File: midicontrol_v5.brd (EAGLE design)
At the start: 118.2 x 42.4 mm, 65 parts, among them SW1 EC12E_SW, U1 6N138S(TB), U3 74HC595D, U4 ATMEGA328P-AN, Y1 CSTCE16M0V53-R0

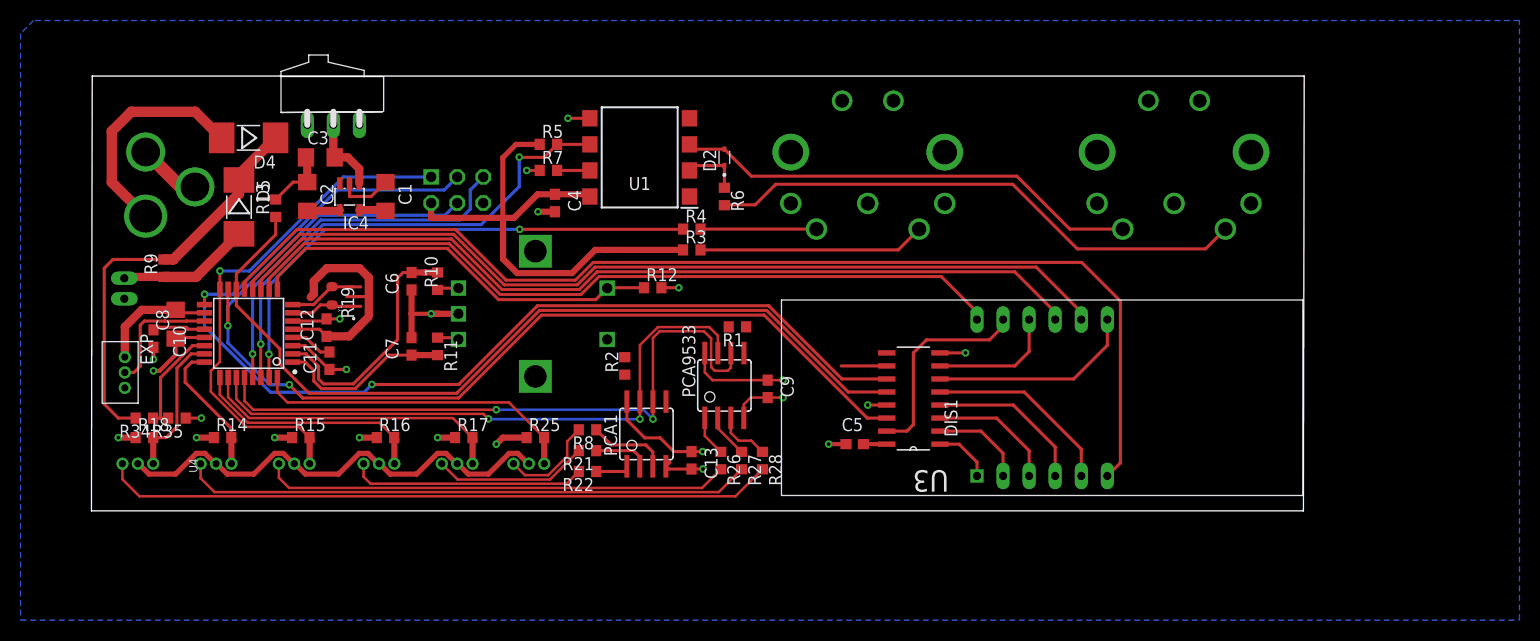
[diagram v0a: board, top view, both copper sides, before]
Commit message: finished midiconrol
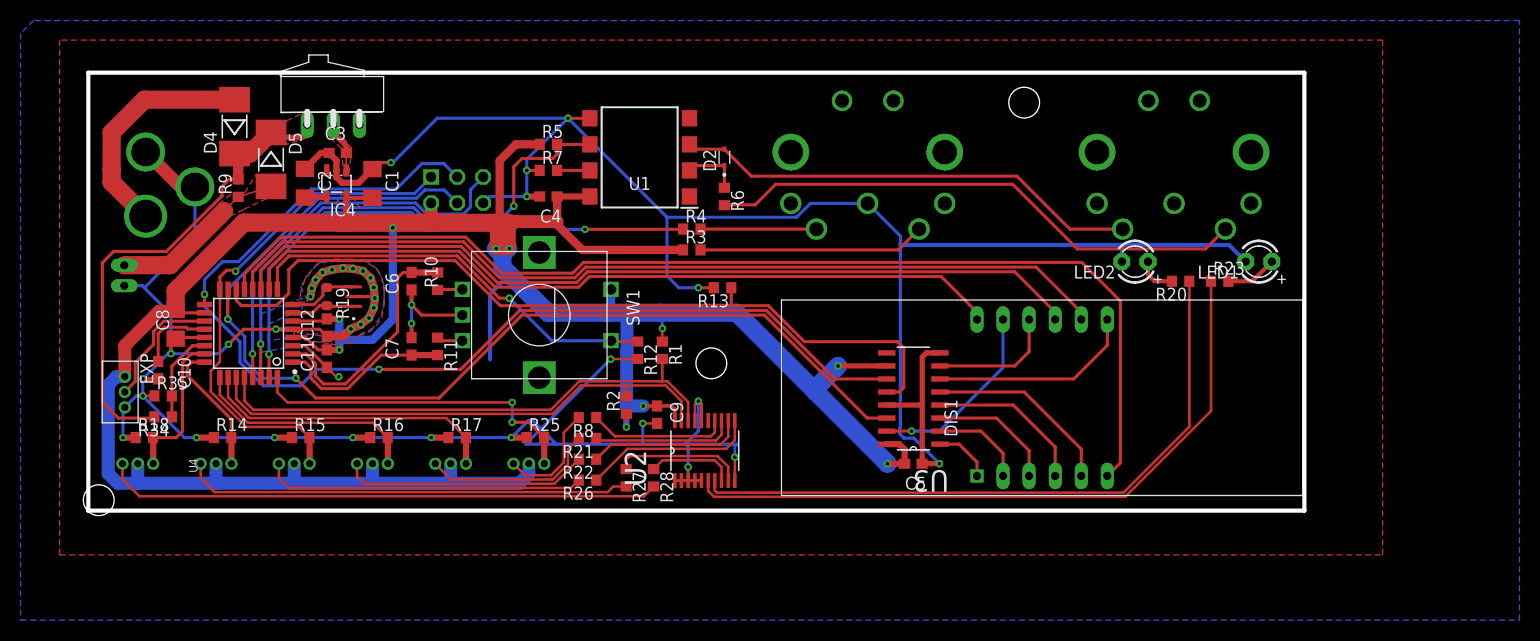
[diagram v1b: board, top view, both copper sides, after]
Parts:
- removed C13: 0.1uf, rcl:C0603
- removed PCA1, PCA9533: PCA9533, adam - ics:SOIC8
- added LED1, LED2: (no value), adafruit:LED3MM
- added R20, R23: 220R, rcl:R0603
- added U2: PCA9634PW,112, PCA9634PW_112:SOP65P640X110-20N
- C3: device rcl:C1206 -> rcl:C0603
- moved R13 44.2 mm to (60.8, 79.4), turned to 180 degrees
- moved R26 13.1 mm to (47.6, 60.6), turned to 180 degrees
- moved R27 11.4 mm to (51.4, 60.9)
- moved C9 11.1 mm to (54.4, 67.0)
- moved R28 10.7 mm to (54.1, 60.9)
- moved R9 10.6 mm to (13.6, 89.1)
- moved R1 7.66 mm to (54.9, 73.3), turned to 270 degrees
- moved R12 6.27 mm to (52.5, 73.3), turned to 270 degrees
- moved C5 6.02 mm to (79.4, 62.2), turned to 180 degrees
- moved D5 5.58 mm to (16.8, 91.9)
- moved R2 3.81 mm to (51.4, 67.9)
- moved C10 3.11 mm to (5.79, 71.3)
- moved R35 2.54 mm to (6.27, 68.8), turned to 0 degrees
- moved EXP 1.91 mm to (2.54, 69.2)
- moved R34 1.83 mm to (6.27, 66.8)
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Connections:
- new net N$30: R28.1, U2.8
- new net N$31: R20.1, U2.7
- new net N$32: R23.1, U2.6
- new net N$33: LED1.A, R23.2
- net +5V: now also U2.20; no longer C13.1, PCA1.8, PCA9533.8
- net ENC_A: now also SW1.A; no longer SW1.B
- net ENC_B: now also SW1.B; no longer SW1.A
- net GND: now also LED1.K, LED2.K, U2.1, U2.10, U2.16, U2.17, U2.2, U2.3, U2.4, U2.5; no longer C13.2, PCA1.4, PCA9533.4
- net N$22: now also LED2.A, R20.2; no longer PCA9533.3, R28.1
- net N$23: now also R8.1, U2.14; no longer PCA9533.2, R27.1
- net N$24: now also R21.1, U2.13; no longer PCA9533.1, R26.1
- net N$27: now also R22.1, U2.12; no longer PCA1.2, R21.1
- net N$28: now also R26.1, U2.11; no longer PCA1.3, R8.1
- net N$29: now also R27.1, U2.9; no longer PCA1.1, R22.1
- net SCL: now also U2.18; no longer PCA1.6, PCA9533.6
- net SDA: now also U2.19; no longer PCA1.7, PCA9533.7
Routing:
- net GND: track 102.1 -> 383.4 mm, vias 20 -> 40
- net +5V: track 148.1 -> 297.3 mm, vias 3 -> 10
- net N$32: track 0.00 -> 66.4 mm
- net N$31: track 0.00 -> 64.1 mm
- net LED_GND_0: track 45.6 -> 31.3 mm
- net LED_GND_1: track 55.6 -> 43.7 mm
- net SCL: track 63.4 -> 51.8 mm, vias 2 -> 0
- net LED_GND_2: track 65.7 -> 54.4 mm
- net N$24: track 3.95 -> 13.9 mm
- net N$27: track 5.42 -> 15.3 mm
- net N$23: track 4.28 -> 13.6 mm
- net N$29: track 3.47 -> 12.8 mm
- net N$28: track 7.81 -> 17.0 mm
- net SDA: track 59.8 -> 50.8 mm, vias 2 -> 0
- net N$30: track 0.00 -> 8.55 mm
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- added copper zone on layer 1, net +5V
- added copper zone on layer 1, net GND
- added copper zone on layer 1, net N$18
- added copper zone on layer 1, net N$26
- added copper zone on layer 1, net PWR
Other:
- board size 118.2 x 42.4 mm -> 118.5 x 42.7 mm
